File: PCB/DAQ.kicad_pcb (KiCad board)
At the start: 2 copper layers, 164 x 140 mm, 45 parts, among them IC1 MAX743CWE+, J1 Arduino_Mega_Header, J10 Conn_01x01, J11 Conn_01x01, J12 Conn_01x01, J2 Conn_01x07, J3 Conn_01x08, J4 Conn_01x08, J5 Conn_02x18_Counter_Clockwise, J6 Conn_01x10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

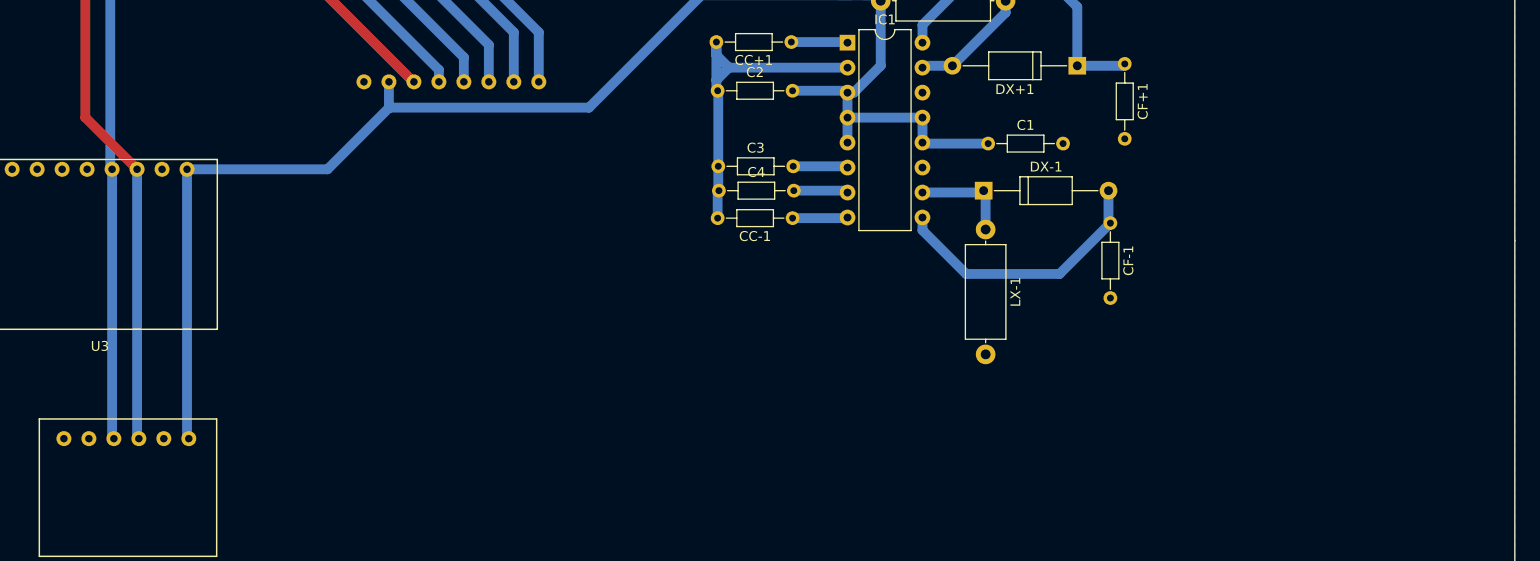
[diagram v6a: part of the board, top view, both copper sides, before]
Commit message: Added analog part of DAC to PCB
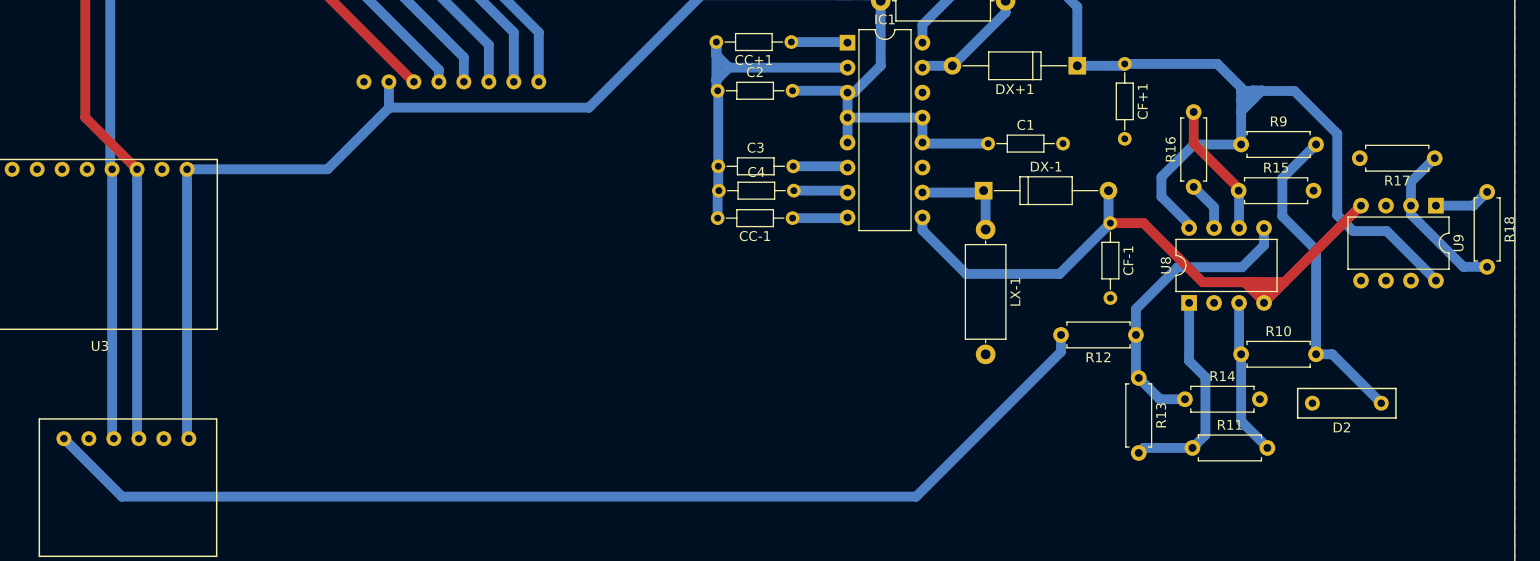
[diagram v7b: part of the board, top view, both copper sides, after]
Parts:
- added D2: LM4040, TH-R:R-C-L-D, F.Cu at (169.4, 143.0)
- added R10: 10K, Resistors_THT:R_Axial_DIN0207_L6.3mm_D2.5mm_P7.62mm_Horizontal, F.Cu at (153.7, 136.5)
- added R11: 10K, Resistors_THT:R_Axial_DIN0207_L6.3mm_D2.5mm_P7.62mm_Horizontal, F.Cu at (148.7, 146.1)
- added R12: 100K, Resistors_THT:R_Axial_DIN0207_L6.3mm_D2.5mm_P7.62mm_Horizontal, F.Cu at (143.0, 134.6)
- added R13: 200K, Resistors_THT:R_Axial_DIN0207_L6.3mm_D2.5mm_P7.62mm_Horizontal, F.Cu at (143.3, 138.9)
- added R14: 57K, Resistors_THT:R_Axial_DIN0207_L6.3mm_D2.5mm_P7.62mm_Horizontal, F.Cu at (148.0, 141.1)
- added R15: 47K, Resistors_THT:R_Axial_DIN0207_L6.3mm_D2.5mm_P7.62mm_Horizontal, F.Cu at (153.4, 119.9)
- added R16: 100K, Resistors_THT:R_Axial_DIN0207_L6.3mm_D2.5mm_P7.62mm_Horizontal, F.Cu at (148.8, 119.5)
- added R17: 50K, Resistors_THT:R_Axial_DIN0207_L6.3mm_D2.5mm_P7.62mm_Horizontal, F.Cu at (173.4, 116.6)
- added R18: 50k, Resistors_THT:R_Axial_DIN0207_L6.3mm_D2.5mm_P7.62mm_Horizontal, F.Cu at (178.7, 120.0)
- added R9: 22K, Resistors_THT:R_Axial_DIN0207_L6.3mm_D2.5mm_P7.62mm_Horizontal, F.Cu at (153.7, 115.2)
- added U8: LM358, Housings_DIP:DIP-8_W7.62mm, F.Cu at (148.4, 131.3)
- added U9: LM358, Housings_DIP:DIP-8_W7.62mm, F.Cu at (173.5, 121.4)
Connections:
- U5 pad 1: Net-(U5-Pad1) -> /DACVo
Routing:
- net /DACVo: track 0.00 -> 111.7 mm
- net /+15V: track 31.8 -> 107.2 mm
- net /-15V: track 63.4 -> 113.5 mm
- net Net-(D2-Pad1): track 0.00 -> 32.9 mm
- net Net-(R12-Pad1): track 0.00 -> 30.2 mm
- net Net-(R11-Pad1): track 0.00 -> 21.7 mm
- net Net-(R17-Pad1): track 0.00 -> 16.7 mm
- net Net-(R10-Pad1): track 0.00 -> 15.9 mm
- net Net-(R15-Pad1): track 0.00 -> 13.7 mm
- net /Vo: track 0.00 -> 5.79 mm
- net Net-(R16-Pad1): track 0.00 -> 5.03 mm
- net /PIN50: track 30.9 -> 33.2 mm
- net Net-(J5-Pad31): track 5.10 -> 2.80 mm
- net /PIN52: track 41.2 -> 43.2 mm
- net Net-(J5-Pad33): track 5.09 -> 3.10 mm

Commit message: Analog parts of the PCB upgraded
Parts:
- R17: value 50K -> 10K
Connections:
- U7 pad 5: Net-(U7-Pad5) -> (no net)
- U7 pad 6: Net-(U7-Pad6) -> (no net)
- U7 pad 7: Net-(U7-Pad7) -> (no net)
- U8 pad 2: Net-(R11-Pad1) -> Net-(R10-Pad1)
- U8 pad 3: Net-(R10-Pad1) -> /GND
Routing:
- net Net-(R16-Pad1): track 5.03 -> 55.0 mm, vias 0 -> 1
- net Net-(R11-Pad1): track 21.7 -> 26.3 mm
- net /GND: track 0.52 -> 3.67 mm
- net Net-(R10-Pad1): track 15.9 -> 17.3 mm
